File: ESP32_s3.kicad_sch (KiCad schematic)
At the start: 65 parts, among them J11 backup, J13 Jetson Power Supply, J14 TXRX, J15 TXRX2, J3 Conn_01x02, J4 Servo motor, J5 PJ-040DH, J7 Conn_01x02, J8 Conn_01x02, J9 Conn_01x02, Q1 BSS138, SW1 SW_Push, SW2 SW_Push, U1 ESP32-S3-WROOM-1-N8R2, U2 LM1117T-ADJ, U3 L298N, U4 TPS61088RHLR

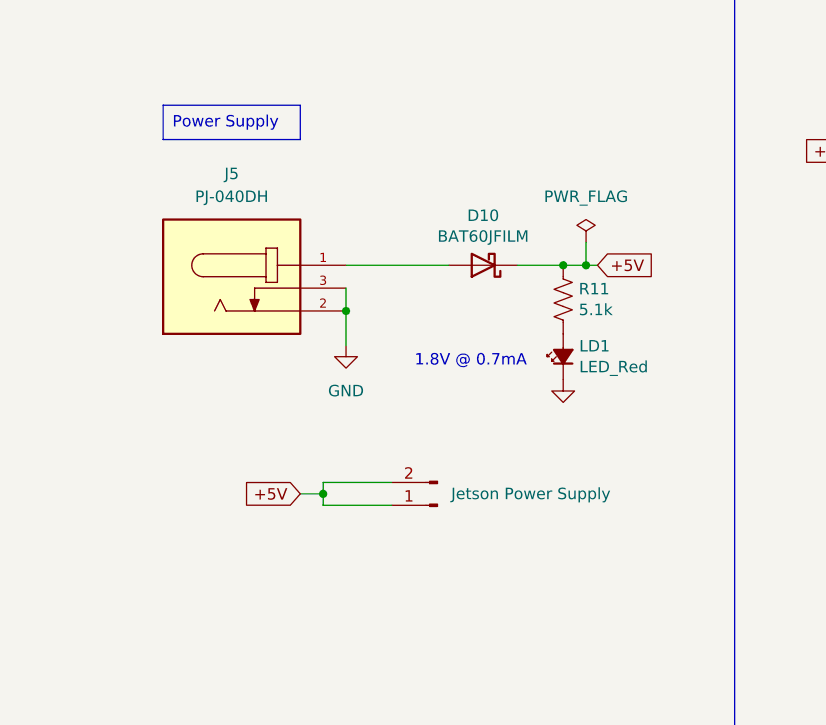
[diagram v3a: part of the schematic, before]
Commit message: change barrel jack
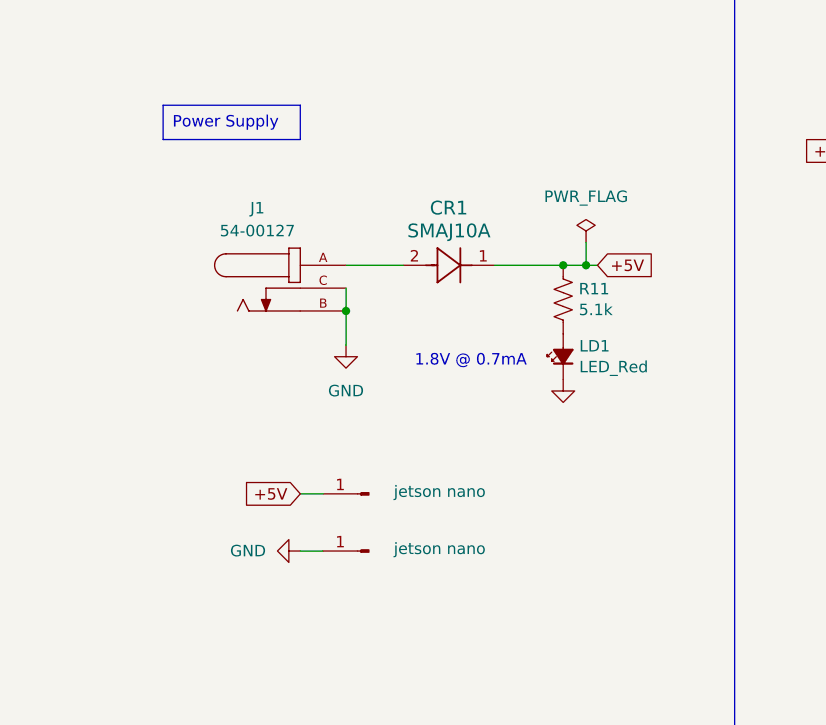
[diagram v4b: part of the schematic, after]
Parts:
- removed D10: BAT60JFILM, Diode_SMD:D_SOD-323, symbol Diode:BAT60A
- removed J13: Jetson Power Supply, 01x02connector:CONN_61300211121_WRE, symbol Connector:Conn_01x02_Pin
- removed J5: PJ-040DH, BarrelJack:CUI_PJ-040DH, symbol PJ-040DH:PJ-040DH
- added CR1: SMAJ10A, SMASeries_LTF, symbol 2024-10-10_19-12-55:SMAJ10A
- added J1: 54-00127, 54-00127:TENSILITY_54-00127, symbol 54-00127:54-00127
- added J2, J5: jetson nano, symbol Connector:Conn_01x01_Pin
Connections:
- net +5V: now also CR1.1, J2.1 (Pin_1)
- net GND: now also J1.B, J1.C, J5.1 (Pin_1)
- new net: CR1.2, J1.A

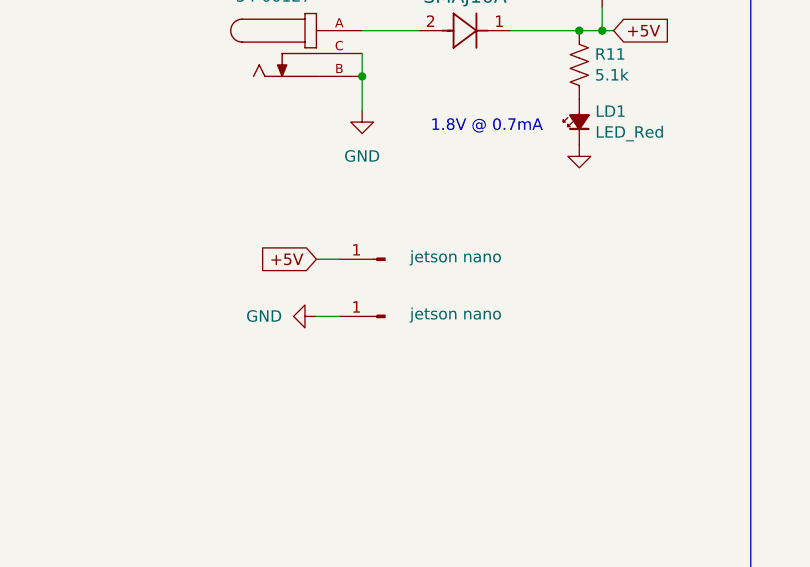
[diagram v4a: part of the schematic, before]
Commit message: footprint fix
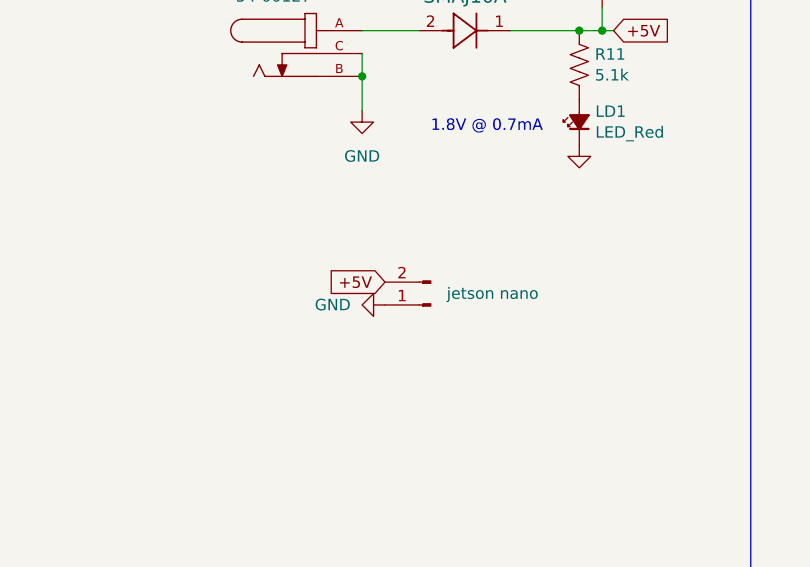
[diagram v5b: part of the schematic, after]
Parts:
- removed J2, J5: jetson nano, symbol Connector:Conn_01x01_Pin
- added J6: jetson nano, 01x02connector:CONN_61300211121_WRE, symbol Connector:Conn_01x02_Pin
- CR1: footprint SMASeries_LTF -> SMAJ10A:SMASeries_LTF
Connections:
- net +5V: now also J6.2 (Pin_2)
- net GND: now also J6.1 (Pin_1)
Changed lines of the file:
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@@
 	(wire
 		(pts
-			(xy 63.5 81.28) (xy 66.04 81.28)
-		)
-		(stroke
-			(width 0)
-			(type default)
-		)
-	)
-	(wire
-		(pts
 			(xy 224.79 72.39) (xy 214.63 72.39)
 		)
@@
 	(wire
 		(pts
-			(xy 63.5 74.93) (xy 66.04 74.93)
-		)
-		(stroke
-			(width 0)
-			(type default)
-		)
-	)
-	(wire
-		(pts
 			(xy 254 215.9) (xy 248.92 215.9)
 		)
@@
 		)
 	)
-	(global_label "+5V"
-		(shape input)
-		(at 63.5 74.93 180)
-		(fields_autoplaced yes)
-		(effects
-			(font
-				(size 1.27 1.27)
-			)
-			(justify right)
-		)
-		(property "Intersheetrefs" "${INTERSHEET_REFS}"
-			(at 56.6443 74.93 0)
-			(effects
-				(font
-					(size 1.27 1.27)
-				)
-				(justify right)
-				(hide yes)
-			)
-		)
-	)
 	(global_label "GPIO12"
 		(shape input)
@@
 	(global_label "+5V"
 		(shape input)
+		(at 71.12 77.47 180)
+		(fields_autoplaced yes)
+		(effects
+			(font
+				(size 1.27 1.27)
+			)
+			(justify right)
+		)
+		(property "Intersheetrefs" "${INTERSHEET_REFS}"
+			(at 64.2643 77.47 0)
+			(effects
+				(font
+					(size 1.27 1.27)
+				)
+				(justify right)
+				(hide yes)
+			)
+		)
+	)
+	(global_label "+5V"
+		(shape input)
 		(at 52.07 149.86 180)
 		(fields_autoplaced yes)
@@
 	)
 	(symbol
+		(lib_id "Connector:Conn_01x02_Pin")
+		(at 76.2 80.01 180)
+		(unit 1)
+		(exclude_from_sim no)
+		(in_bom yes)
+		(on_board yes)
+		(dnp no)
+		(property "Reference" "J6"
+			(at 77.47 77.4699 0)
+			(effects
+				(font
+					(size 1.27 1.27)
+				)
+				(justify right)
+				(hide yes)
+			)
+		)
+		(property "Value" "jetson nano"
+			(at 77.978 78.74 0)
+			(effects
+				(font
+					(size 1.27 1.27)
+				)
+				(justify right)
+			)
+		)
+		(property "Footprint" "01x02connector:CONN_61300211121_WRE"
+			(at 76.2 80.01 0)
+			(effects
+				(font
+					(size 1.27 1.27)
+				)
+				(hide yes)
+			)
+		)
+		(property "Datasheet" "~"
+			(at 76.2 80.01 0)
+			(effects
+				(font
+					(size 1.27 1.27)
+				)
+				(hide yes)
+			)
+		)
+		(property "Description" "Generic connector, single row, 01x02, script generated"
+			(at 76.2 80.01 0)
+			(effects
+				(font
+					(size 1.27 1.27)
+				)
+				(hide yes)
+			)
+		)
+		(pin "1"
+		)
+		(pin "2"
+		)
+		(instances
+			(project "ESP32_s3"
+				(path "/17b1a26b-4dd3-45da-ac9f-9f7d4372170f"
+					(reference "J6")
+					(unit 1)
+				)
+			)
+		)
+	)
+	(symbol
 		(lib_id "Driver_Motor:L298N")
 		(at 80.01 245.11 0)
@@
 	(symbol
 		(lib_id "power:GND")
+		(at 71.12 80.01 270)
+		(unit 1)
+		(exclude_from_sim no)
+		(in_bom yes)
+		(on_board yes)
+		(dnp no)
+		(fields_autoplaced yes)
+		(property "Reference" "#PWR02"
+			(at 64.77 80.01 0)
+			(effects
+				(font
+					(size 1.27 1.27)
+				)
+				(hide yes)
+			)
+		)
+		(property "Value" "GND"
+			(at 67.31 80.0099 90)
+			(effects
+				(font
+					(size 1.27 1.27)
+				)
+				(justify right)
+			)
+		)
+		(property "Footprint" ""
+			(at 71.12 80.01 0)
+			(effects
+				(font
+					(size 1.27 1.27)
+				)
+				(hide yes)
+			)
+		)
+		(property "Datasheet" ""
+			(at 71.12 80.01 0)
+			(effects
+				(font
+					(size 1.27 1.27)
+				)
+				(hide yes)
+			)
+		)
+		(property "Description" "Power symbol creates a global label with name \"GND\" , ground"
+			(at 71.12 80.01 0)
+			(effects
+				(font
+					(size 1.27 1.27)
+				)
+				(hide yes)
+			)
+		)
+		(pin "1"
+		)
+		(instances
+			(project "ESP32_s3"
+				(path "/17b1a26b-4dd3-45da-ac9f-9f7d4372170f"
+					(reference "#PWR02")
+					(unit 1)
+				)
+			)
+		)
+	)
+	(symbol
+		(lib_id "power:GND")
 		(at 369.57 229.87 270)
 		(unit 1)
@@
 			)
 		)
-		(property "Footprint" "SMASeries_LTF"
+		(property "Footprint" "SMAJ10A:SMASeries_LTF"
 			(at 74.93 49.53 0)
 			(effects
@@
 	)
 	(symbol
-		(lib_id "Connector:Conn_01x01_Pin")
-		(at 71.12 74.93 180)
-		(unit 1)
-		(exclude_from_sim no)
-		(in_bom yes)
-		(on_board yes)
-		(dnp no)
-		(property "Reference" "J2"
-			(at 70.485 69.85 0)
-			(effects
-				(font
-					(size 1.27 1.27)
-				)
-				(hide yes)
-			)
-		)
-		(property "Value" "jetson nano"
-			(at 78.994 74.676 0)
-			(effects
-				(font
-					(size 1.27 1.27)
-				)
-			)
-		)
-		(property "Footprint" ""
-			(at 71.12 74.93 0)
-			(effects
-				(font
-					(size 1.27 1.27)
-				)
-				(hide yes)
-			)
-		)
-		(property "Datasheet" "~"
-			(at 71.12 74.93 0)
-			(effects
-				(font
-					(size 1.27 1.27)
-				)
-				(hide yes)
-			)
-		)
-		(property "Description" "Generic connector, single row, 01x01, script generated"
-			(at 71.12 74.93 0)
-			(effects
-				(font
-					(size 1.27 1.27)
-				)
-				(hide yes)
-			)
-		)
-		(pin "1"
-		)
-		(instances
-			(project "ESP32_s3"
-				(path "/17b1a26b-4dd3-45da-ac9f-9f7d4372170f"
-					(reference "J2")
-					(unit 1)
-				)
-			)
-		)
-	)
-	(symbol
 		(lib_id "Device:R")
 		(at 87.63 163.83 0)
@@
 	)
 	(symbol
-		(lib_id "Connector:Conn_01x01_Pin")
-		(at 71.12 81.28 180)
-		(unit 1)
-		(exclude_from_sim no)
-		(in_bom yes)
-		(on_board yes)
-		(dnp no)
-		(property "Reference" "J5"
-			(at 70.485 76.2 0)
-			(effects
-				(font
-					(size 1.27 1.27)
-				)
-				(hide yes)
-			)
-		)
-		(property "Value" "jetson nano"
-			(at 78.994 81.026 0)
-			(effects
-				(font
-					(size 1.27 1.27)
-				)
-			)
-		)
-		(property "Footprint" ""
-			(at 71.12 81.28 0)
-			(effects
-				(font
-					(size 1.27 1.27)
-				)
-				(hide yes)
-			)
-		)
-		(property "Datasheet" "~"
-			(at 71.12 81.28 0)
-			(effects
-				(font
-					(size 1.27 1.27)
-				)
-				(hide yes)
-			)
-		)
-		(property "Description" "Generic connector, single row, 01x01, script generated"
-			(at 71.12 81.28 0)
-			(effects
-				(font
-					(size 1.27 1.27)
-				)
-				(hide yes)
-			)
-		)
-		(pin "1"
-		)
-		(instances
-			(project "ESP32_s3"
-				(path "/17b1a26b-4dd3-45da-ac9f-9f7d4372170f"
-					(reference "J5")
-					(unit 1)
-				)
-			)
-		)
-	)
-	(symbol
 		(lib_id "Device:C")
 		(at 353.06 43.18 270)
@@
 					(unit 1)
 				)
-			)
-		)
-	)
-	(symbol
-		(lib_id "power:GND")
-		(at 63.5 81.28 270)
-		(unit 1)
-		(exclude_from_sim no)
-		(in_bom yes)
-		(on_board yes)
-		(dnp no)
-		(fields_autoplaced yes)
-		(property "Reference" "#PWR02"
-			(at 57.15 81.28 0)
-			(effects
-				(font
-					(size 1.27 1.27)
-				)
-				(hide yes)
-			)
-		)
-		(property "Value" "GND"
-			(at 59.69 81.2799 90)
-			(effects
-				(font
-					(size 1.27 1.27)
-				)
-				(justify right)
-			)
-		)
-		(property "Footprint" ""
-			(at 63.5 81.28 0)
-			(effects
-				(font
-					(size 1.27 1.27)
-				)
-				(hide yes)
-			)
-		)
-		(property "Datasheet" ""
-			(at 63.5 81.28 0)
-			(effects
-				(font
-					(size 1.27 1.27)
-				)
-				(hide yes)
-			)
-		)
-		(property "Description" "Power symbol creates a global label with name \"GND\" , ground"
-			(at 63.5 81.28 0)
-			(effects
-				(font
-					(size 1.27 1.27)
-				)
-				(hide yes)
-			)
-		)
-		(pin "1"
-		)
-		(instances
-			(project "ESP32_s3"
-				(path "/17b1a26b-4dd3-45da-ac9f-9f7d4372170f"
-					(reference "#PWR02")
-					(unit 1)
-				)

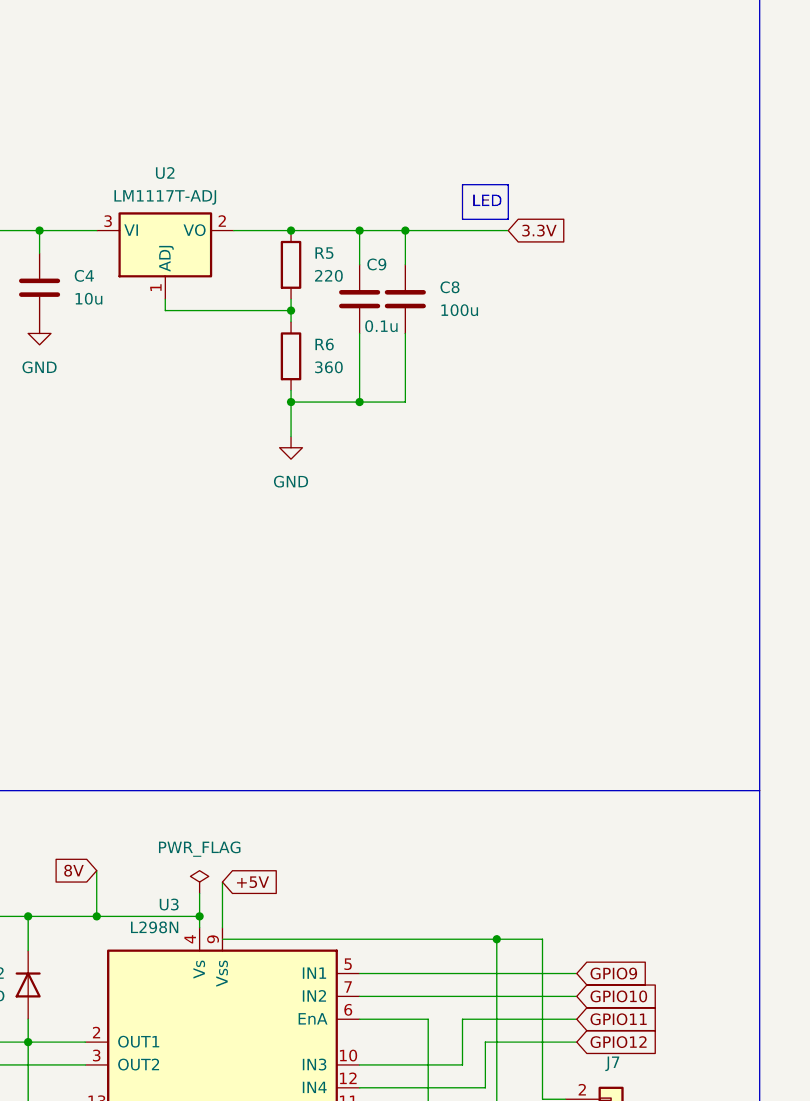
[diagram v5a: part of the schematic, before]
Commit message: update schematic and layout
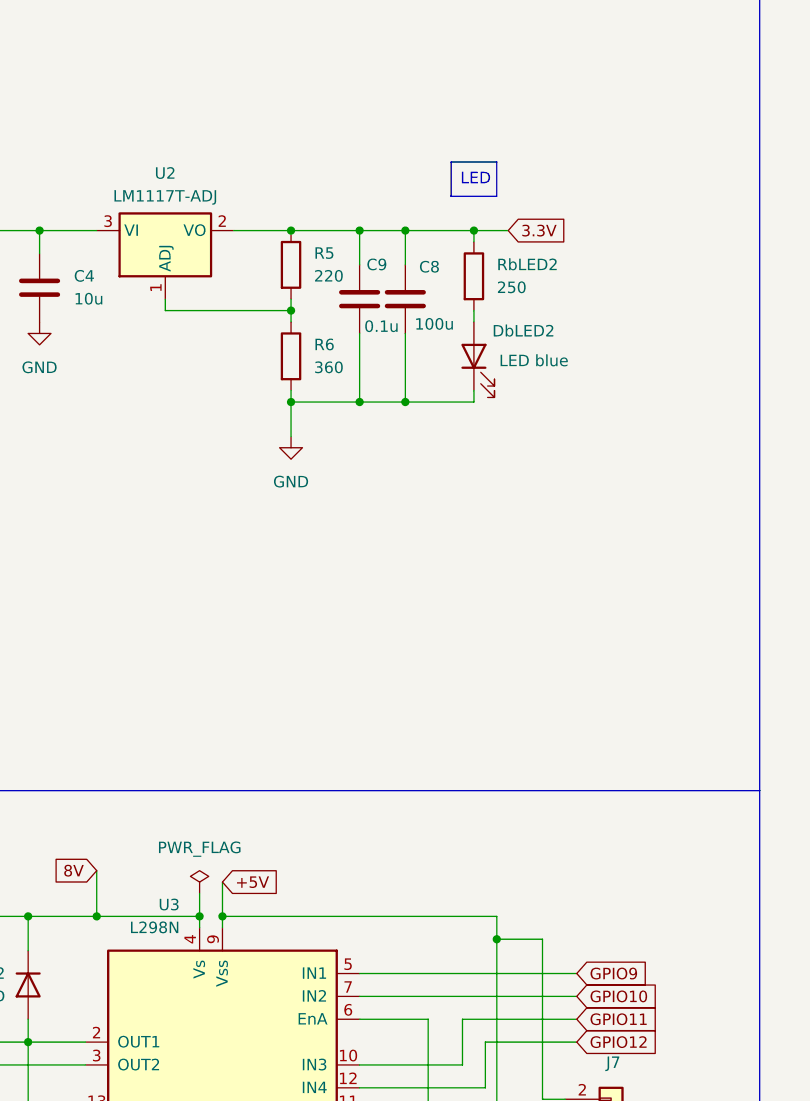
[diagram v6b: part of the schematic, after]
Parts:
- added DbLED2: LED blue, WL-SMCW_0805:WL-SMCW_0805, symbol Device:LED
- added RbLED2: 250, CRCW080535K7FKEA:RESC2012X50N, symbol Device:R
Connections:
- net +5V: now also J3.2 (Pin_2), J7.2 (Pin_2)
- net 3.3V: now also RbLED2.1
- net GND: now also DbLED2.1 (K)
- new net: DbLED2.2 (A), RbLED2.2
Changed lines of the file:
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@@
 	)
 	(junction
+		(at 80.01 226.06)
+		(diameter 0)
+		(color 0 0 0 0)
+	)
+	(junction
 		(at 87.63 149.86)
 		(diameter 0)
@@
 	)
 	(junction
+		(at 100.33 168.91)
+		(diameter 0)
+		(color 0 0 0 0)
+	)
+	(junction
 		(at 58.42 240.03)
 		(diameter 0)
@@
 	)
 	(junction
+		(at 107.95 149.86)
+		(diameter 0)
+		(color 0 0 0 0)
+	)
+	(junction
 		(at 58.42 226.06)
 		(diameter 0)
@@
 	)
 	(junction
+		(at 110.49 228.6)
+		(diameter 0)
+		(color 0 0 0 0)
+	)
+	(junction
 		(at 302.26 67.31)
 		(diameter 0)
@@
 	)
 	(junction
-		(at 110.49 228.6)
-		(diameter 0)
-		(color 0 0 0 0)
-	)
-	(junction
 		(at 369.57 224.79)
 		(diameter 0)
@@
 	(wire
 		(pts
+			(xy 80.01 226.06) (xy 110.49 226.06)
+		)
+		(stroke
+			(width 0)
+			(type default)
+		)
+	)
+	(wire
+		(pts
 			(xy 194.31 74.93) (xy 194.31 78.74)
 		)
@@
 	(wire
 		(pts
+			(xy 107.95 167.64) (xy 107.95 168.91)
+		)
+		(stroke
+			(width 0)
+			(type default)
+		)
+	)
+	(wire
+		(pts
+			(xy 100.33 168.91) (xy 107.95 168.91)
+		)
+		(stroke
+			(width 0)
+			(type default)
+		)
+	)
+	(wire
+		(pts
 			(xy 203.2 182.88) (xy 208.28 182.88)
 		)
@@
 	(wire
 		(pts
+			(xy 107.95 151.13) (xy 107.95 149.86)
+		)
+		(stroke
+			(width 0)
+			(type default)
+		)
+	)
+	(wire
+		(pts
 			(xy 260.35 77.47) (xy 266.7 77.47)
 		)
@@
 	(wire
 		(pts
+			(xy 110.49 228.6) (xy 110.49 226.06)
+		)
+		(stroke
+			(width 0)
+			(type default)
+		)
+	)
+	(wire
+		(pts
 			(xy 260.35 85.09) (xy 260.35 90.17)
 		)
@@
 	(wire
 		(pts
+			(xy 80.01 226.06) (xy 80.01 227.33)
+		)
+		(stroke
+			(width 0)
+			(type default)
+		)
+	)
+	(wire
+		(pts
 			(xy 204.47 86.36) (xy 204.47 97.79)
 		)
@@
 	(wire
 		(pts
+			(xy 107.95 158.75) (xy 107.95 160.02)
+		)
+		(stroke
+			(width 0)
+			(type default)
+		)
+	)
+	(wire
+		(pts
 			(xy 252.73 177.8) (xy 252.73 175.26)
 		)
@@
 	(wire
 		(pts
+			(xy 107.95 149.86) (xy 111.76 149.86)
+		)
+		(stroke
+			(width 0)
+			(type default)
+		)
+	)
+	(wire
+		(pts
 			(xy 350.52 208.28) (xy 350.52 209.55)
 		)
@@
 	(wire
 		(pts
-			(xy 100.33 149.86) (xy 111.76 149.86)
+			(xy 100.33 149.86) (xy 107.95 149.86)
 		)
 		(stroke
@@
 	(wire
 		(pts
-			(xy 80.01 228.6) (xy 110.49 228.6)
-		)
-		(stroke
-			(width 0)
-			(type default)
-		)
-	)
-	(wire
-		(pts
 			(xy 203.2 185.42) (xy 208.28 185.42)
 		)
@@
 	(wire
 		(pts
-			(xy 80.01 222.25) (xy 80.01 227.33)
+			(xy 80.01 222.25) (xy 80.01 226.06)
 		)
 		(stroke
@@
 	(text_box "LED \n"
 		(exclude_from_sim no)
-		(at 106.68 144.78 0)
+		(at 105.41 142.24 0)
 		(size 5.08 3.81)
 		(stroke
@@
 		(on_board yes)
 		(dnp no)
-		(fields_autoplaced yes)
 		(property "Reference" "C8"
-			(at 104.14 156.2099 0)
+			(at 101.854 153.924 0)
 			(effects
 				(font
@@
 		)
 		(property "Value" "100u"
-			(at 104.14 158.7499 0)
+			(at 101.346 160.274 0)
 			(effects
 				(font
@@
 	)
 	(symbol
+		(lib_id "Device:LED")
+		(at 107.95 163.83 90)
+		(unit 1)
+		(exclude_from_sim no)
+		(in_bom yes)
+		(on_board yes)
+		(dnp no)
+		(property "Reference" "DbLED2"
+			(at 109.982 161.036 90)
+			(effects
+				(font
+					(size 1.27 1.27)
+				)
+				(justify right)
+			)
+		)
+		(property "Value" "LED blue"
+			(at 110.744 164.338 90)
+			(effects
+				(font
+					(size 1.27 1.27)
+				)
+				(justify right)
+			)
+		)
+		(property "Footprint" "WL-SMCW_0805:WL-SMCW_0805"
+			(at 107.95 163.83 0)
+			(effects
+				(font
+					(size 1.27 1.27)
+				)
+				(hide yes)
+			)
+		)
+		(property "Datasheet" "https://www.we-online.com/components/products/datasheet/150080BS75000.pdf"
+			(at 107.95 163.83 0)
+			(effects
+				(font
+					(size 1.27 1.27)
+				)
+				(hide yes)
+			)
+		)
+		(property "Description" "Light emitting diode"
+			(at 107.95 163.83 0)
+			(effects
+				(font
+					(size 1.27 1.27)
+				)
+				(hide yes)
+			)
+		)
+		(pin "2"
+		)
+		(pin "1"
+		)
+		(instances
+			(project "ESP32_s3"
+				(path "/17b1a26b-4dd3-45da-ac9f-9f7d4372170f"
+					(reference "DbLED2")
+					(unit 1)
+				)
+			)
+		)
+	)
+	(symbol
 		(lib_id "power:GND")
 		(at 87.63 172.72 0)
@@
 					(unit 1)
 				)
+			)
+		)
+	)
+	(symbol
+		(lib_id "Device:R")
+		(at 107.95 154.94 0)
+		(unit 1)
+		(exclude_from_sim no)
+		(in_bom yes)
+		(on_board yes)
+		(dnp no)
+		(property "Reference" "RbLED2"
+			(at 110.49 153.6699 0)
+			(effects
+				(font
+					(size 1.27 1.27)
+				)
+				(justify left)
+			)
+		)
+		(property "Value" "250"
+			(at 110.49 156.2099 0)
+			(effects
+				(font
+					(size 1.27 1.27)
+				)
+				(justify left)
+			)
+		)
+		(property "Footprint" "CRCW080535K7FKEA:RESC2012X50N"
+			(at 106.172 154.94 90)
+			(effects
+				(font
+					(size 1.27 1.27)
+				)
+				(hide yes)
+			)
+		)
+		(property "Datasheet" "https://www.seielect.com/catalog/sei-rncf.pdf"
+			(at 107.95 154.94 0)
+			(effects
+				(font
+					(size 1.27 1.27)
+				)
+				(hide yes)
+			)
+		)
+		(property "Description" "Resistor"
+			(at 107.95 154.94 0)
+			(effects
+				(font
+					(size 1.27 1.27)
+				)
+				(hide yes)
+			)
+		)
+		(pin "1"
+		)
+		(pin "2"
+		)
+		(instances
+			(project "ESP32_s3"
+				(path "/17b1a26b-4dd3-45da-ac9f-9f7d4372170f"
+					(reference "RbLED2")
+					(unit 1)
+				)

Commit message: layout v1
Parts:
- removed R7: 16, CRGCQ0805F220R:RESC2012X65N, symbol Device:R_US
- added H1, H2, H3, H4: MountingHole, symbol Mechanical:MountingHole
- added NT1: NetTie_2, symbol Device:NetTie_2
- added R2: 16, CRGCQ0805F220R:RESC2012X65N, symbol Device:R_US
- U4: footprint TPS61088RHLR:RHL0020A -> TPS61088RHLR:IC_TPS61088RHLR
- renumbered D6 to D4, D7 to D5, D4 to D6, D5 to D7
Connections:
- net +5V: no longer J3.2 (Pin_2), J7.2 (Pin_2)
- net 3.3V: now also J3.2 (Pin_2), J7.2 (Pin_2)
- net GND: now also NT1.2, R2.1; no longer C7.2, Ccomp1.2, Ccomp2.2, Cin1.2, Cin2.2, Cout1.2, Css1.2, Cvcc1.2, D3.2 (A), D5.2 (A), D7.2 (A), D9.2 (A), DbLED1.1 (K), DrLED1.1 (K), Rfbb1.2, Rlim1.2, U3.1 (SENSE_A), U3.8 (GND), U4.11 (NC), U4.12 (NC), U4.20 (AGND), U4.21 (PGND)
- net GPIO10: now also U3.5 (IN1); no longer U3.7 (IN2)
- net GPIO11: no longer U3.10 (IN3)
- net GPIO12: no longer U3.12 (IN4)
- net GPIO20: now also LD2.2 (A)
- net GPIO3: now also U3.10 (IN3)
- net GPIO35: now also J11.2 (Pin_2)
- net GPIO36: now also J11.1 (Pin_1)
- net GPIO38: no longer LD2.2 (A)
- net GPIO41: no longer J11.1 (Pin_1)
- net GPIO42: no longer J11.2 (Pin_2)
- net GPIO46: now also U3.12 (IN4)
- net GPIO9: now also U3.7 (IN2); no longer U3.5 (IN1)
- net at LD2.1 (K): now also R2.2
- net INPUT V: now reaches CR1.2, J1.A
- new net PGND: C7.2, Ccomp1.2, Ccomp2.2, Cin1.2, Cin2.2, Cout1.2, Css1.2, Cvcc1.2, D3.2 (A), D5.2 (A), D7.2 (A), D9.2 (A), DbLED1.1 (K), DrLED1.1 (K), NT1.1, Rfbb1.2, Rlim1.2, U3.1 (SENSE_A), U3.8 (GND), U4.11 (NC), U4.12 (NC), U4.20 (AGND), U4.21 (PGND)
- no-connect marks 28 -> 24
